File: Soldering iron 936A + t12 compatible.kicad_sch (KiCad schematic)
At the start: 62 parts, among them J1 DC INPUT, J2 OLED, J3 AC input, J4 output_connector, J5 mosfet_driver_future_backup, Q1 IRF9540N, Q2 BC547, SW1 RotaryEncoder_Switch, U1 LM2596S-ADJ, U2 LM358

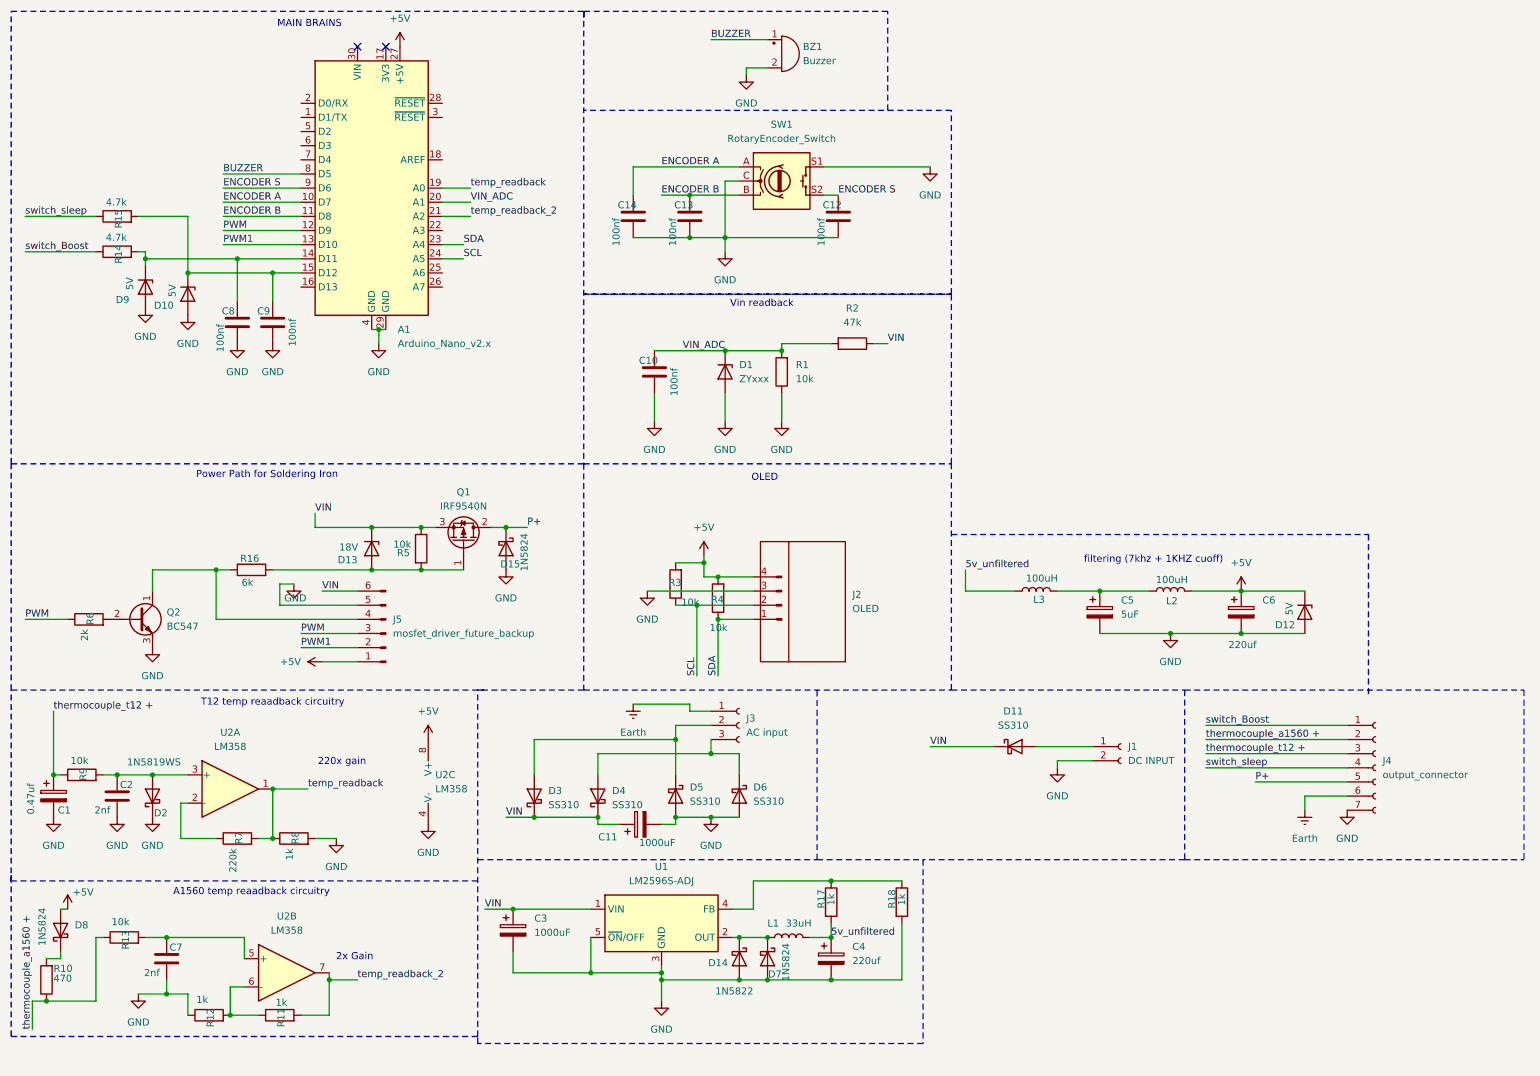
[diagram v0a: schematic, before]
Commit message: PCB arrived , T12 verified , code updating , Fixed mistakes and redid schmatic
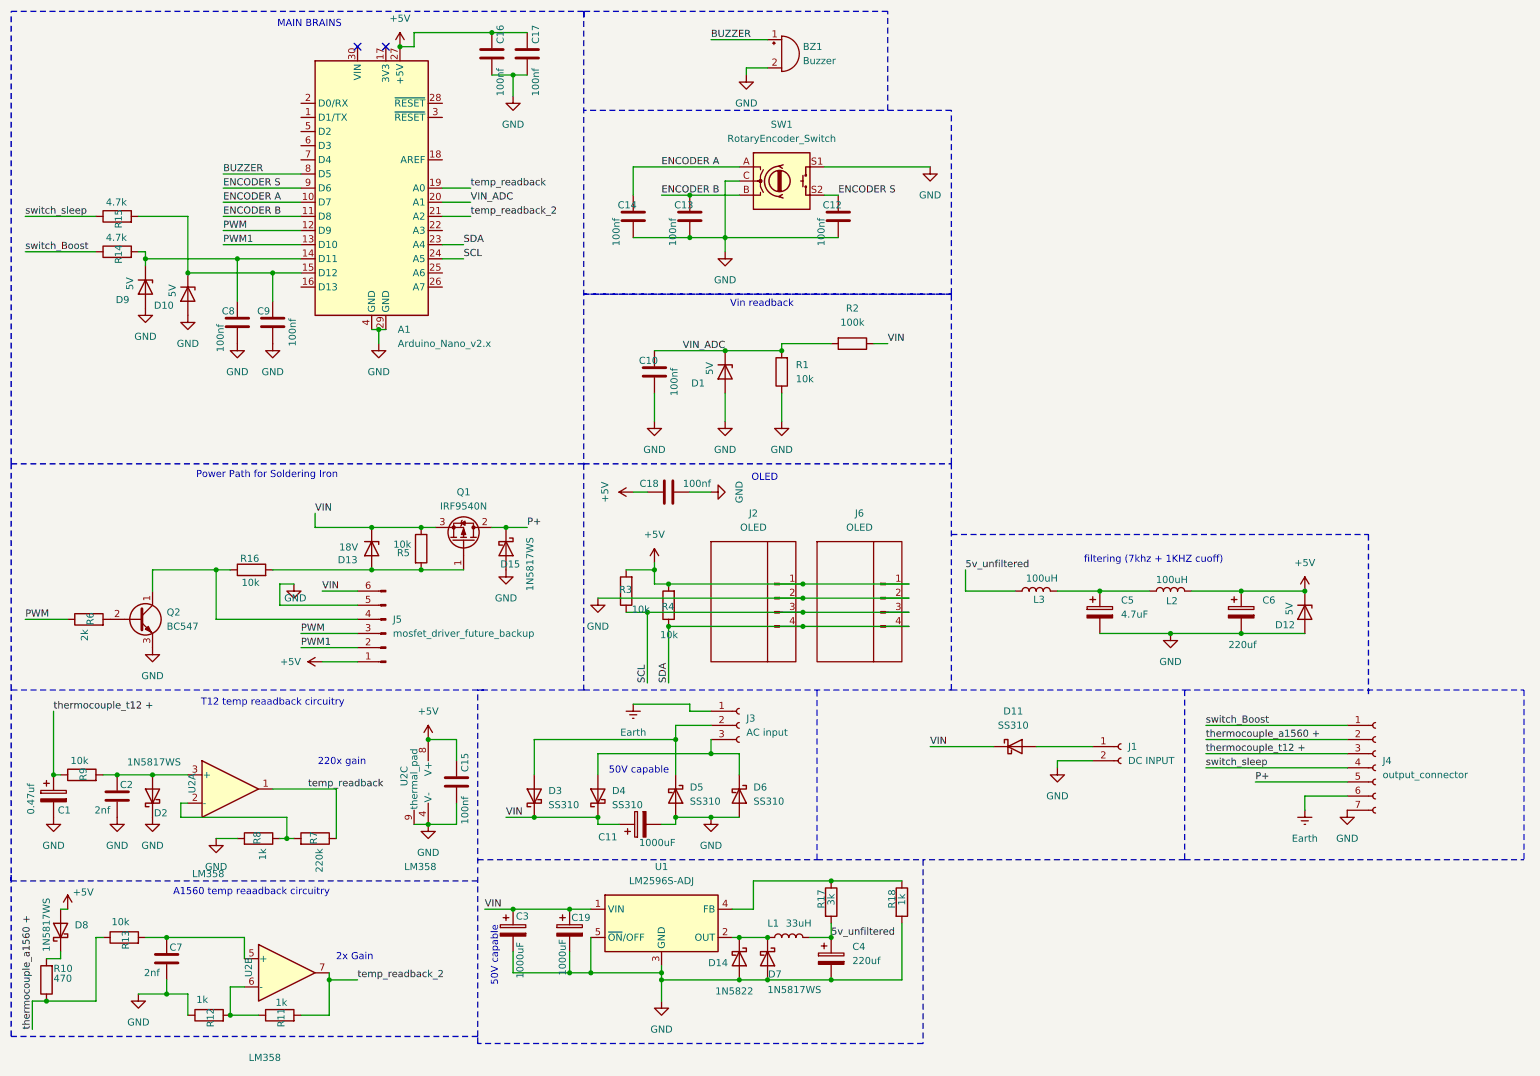
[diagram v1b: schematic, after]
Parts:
- removed D1: ZYxxx, Diode_THT:D_DO-41_SOD81_P10.16mm_Horizontal, symbol Diode:ZYxxx
- added C15, C16, C17, C18: 100nf, Capacitor_SMD:C_0603_1608Metric_Pad1.08x0.95mm_HandSolder, symbol Device:C
- added C19: 1000uF, Capacitor_THT:CP_Radial_D10.0mm_P5.00mm, symbol Device:C_Polarized
- added D1: 5V, Diode_THT:D_A-405_P10.16mm_Horizontal, symbol Device:D_Zener
- added J6: OLED, Connector_PinHeader_2.54mm:PinHeader_1x04_P2.54mm_Vertical, symbol Connector:Conn_01x04_Pin
- C5: value 5uF -> 4.7uF
- D15, D7, D8: value 1N5824 -> 1N5817WS
- D2: value 1N5819WS -> 1N5817WS
- R16: value 6k -> 10k
- R17: value 1k -> 3k
- R2: value 47k -> 100k
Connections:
- net +5V: now also J2.1 (SDA), C15.1, C16.1, C17.1, C18.1, J6.1 (SDA); no longer J2.4 (VDD)
- net GND: now also J2.2 (SCL), U2.9 (thermal_pad), C15.2, C16.2, C17.2, C18.2, C19.2, D1.2 (A), J6.2 (SCL); no longer J2.3 (GND)
- net SCL: now also J2.3 (GND), J6.3 (GND); no longer J2.2 (SCL)
- net SDA: now also J2.4 (VDD), J6.4 (VDD); no longer J2.1 (SDA)
- net VIN: now also C19.1
- net VIN_ADC: now also D1.1 (K)
- net temp_readback: now also R7.1; no longer R7.2, R8.1
- net at U2.2 (-): now also R7.2, R8.1; no longer R7.1
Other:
- note added: "50V capable"
- moved on the sheet: J2, R3, R4, R7, R8

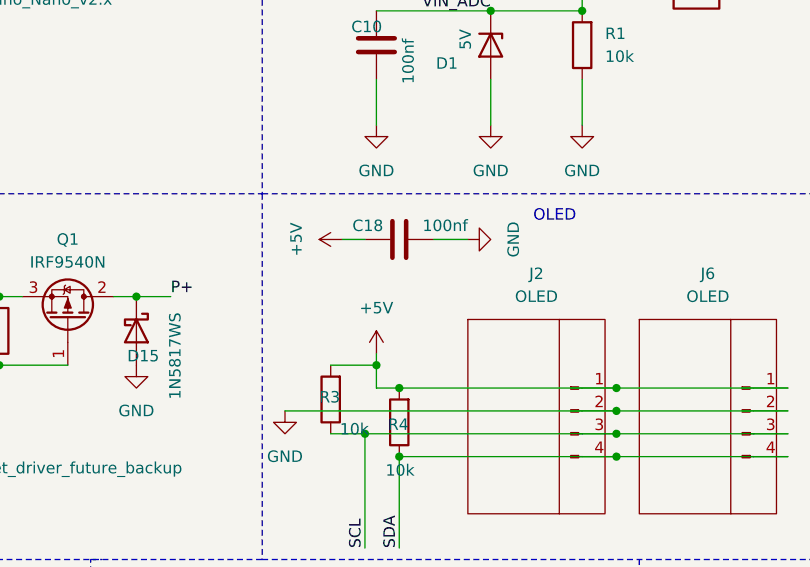
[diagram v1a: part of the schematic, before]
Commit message: added BOM generation + decoupling Cap for other orination of OLED , Fixed PCB orientation in Readme
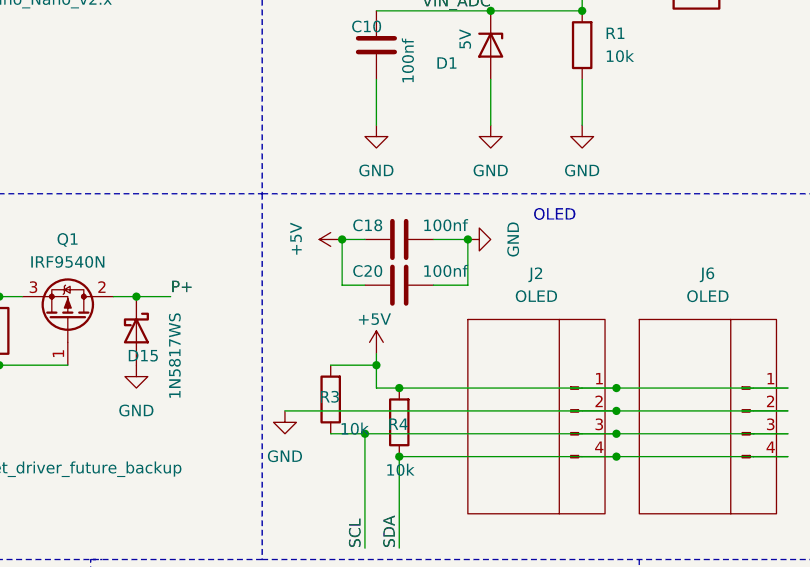
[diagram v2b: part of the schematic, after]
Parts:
- added C20: 100nf, Capacitor_SMD:C_0603_1608Metric_Pad1.08x0.95mm_HandSolder, symbol Device:C
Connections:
- net +5V: now also C20.1
- net GND: now also C20.2
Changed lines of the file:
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@@
 	)
 	(junction
+		(at 138.43 99.06)
+		(diameter 0)
+		(color 0 0 0 0)
+	)
+	(junction
 		(at 132.08 157.48)
 		(diameter 0)
@@
 	)
 	(junction
+		(at 124.46 99.06)
+		(diameter 0)
+		(color 0 0 0 0)
+	)
+	(junction
 		(at 127 120.65)
 		(diameter 0)
@@
 	(wire
 		(pts
+			(xy 127 104.14) (xy 124.46 104.14)
+		)
+		(stroke
+			(width 0)
+			(type default)
+		)
+	)
+	(wire
+		(pts
 			(xy 15.24 49.53) (xy 27.94 49.53)
 		)
@@
 	(wire
 		(pts
+			(xy 138.43 104.14) (xy 138.43 99.06)
+		)
+		(stroke
+			(width 0)
+			(type default)
+		)
+	)
+	(wire
+		(pts
 			(xy 36.83 57.15) (xy 53.34 57.15)
 		)
@@
 	(wire
 		(pts
+			(xy 124.46 104.14) (xy 124.46 99.06)
+		)
+		(stroke
+			(width 0)
+			(type default)
+		)
+	)
+	(wire
+		(pts
 			(xy 40.64 186.69) (xy 40.64 189.23)
 		)
@@
 	(wire
 		(pts
+			(xy 134.62 104.14) (xy 138.43 104.14)
+		)
+		(stroke
+			(width 0)
+			(type default)
+		)
+	)
+	(wire
+		(pts
 			(xy 59.69 59.69) (xy 64.77 59.69)
 		)
@@
 		(on_board yes)
 		(dnp no)
-		(fields_autoplaced yes)
 		(property "Reference" "#PWR09"
 			(at 128.27 115.57 0)
@@
 		)
 		(property "Value" "+5V"
-			(at 128.27 106.68 0)
+			(at 128.016 107.95 0)
 			(effects
 				(font
@@
 					(unit 1)
 				)
+			)
+		)
+	)
+	(symbol
+		(lib_id "Device:C")
+		(at 130.81 104.14 90)
+		(unit 1)
+		(exclude_from_sim no)
+		(in_bom yes)
+		(on_board yes)
+		(dnp no)
+		(property "Reference" "C20"
+			(at 129.032 102.616 90)
+			(effects
+				(font
+					(size 1.27 1.27)
+				)
+				(justify left)
+			)
+		)
+		(property "Value" "100nf"
+			(at 138.43 102.616 90)
+			(effects
+				(font
+					(size 1.27 1.27)
+				)
+				(justify left)
+			)
+		)
+		(property "Footprint" "Capacitor_SMD:C_0603_1608Metric_Pad1.08x0.95mm_HandSolder"
+			(at 134.62 103.1748 0)
+			(effects
+				(font
+					(size 1.27 1.27)
+				)
+				(hide yes)
+			)
+		)
+		(property "Datasheet" "~"
+			(at 130.81 104.14 0)
+			(effects
+				(font
+					(size 1.27 1.27)
+				)
+				(hide yes)
+			)
+		)
+		(property "Description" "Unpolarized capacitor"
+			(at 130.81 104.14 0)
+			(effects
+				(font
+					(size 1.27 1.27)
+				)
+				(hide yes)
+			)
+		)
+		(pin "1"
+		)
+		(pin "2"
+		)
+		(instances
+			(project "Soldering iron 936A + t12 compatible"
+				(path "/7b8f23b9-5775-45f1-8dbe-ed5fada41d3e"
+					(reference "C20")
+					(unit 1)
+				)

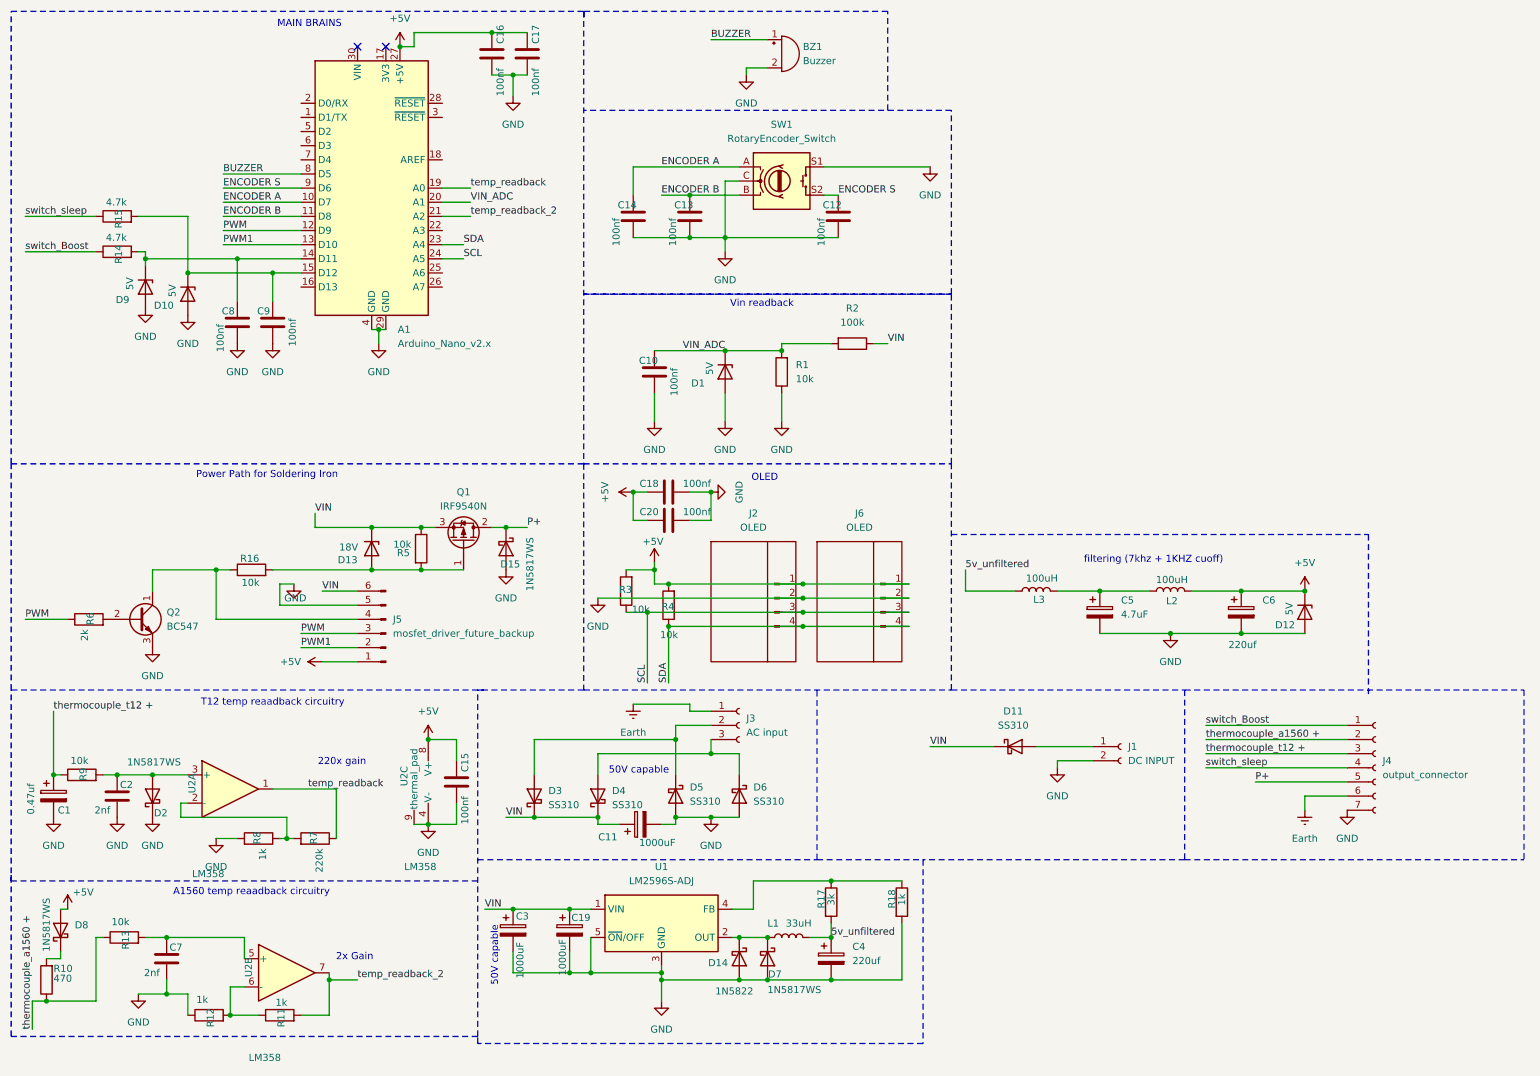
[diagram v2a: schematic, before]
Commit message: Updated schematic but have to update layout , foot prints ,add mosfet driver for 31 KHZ driving
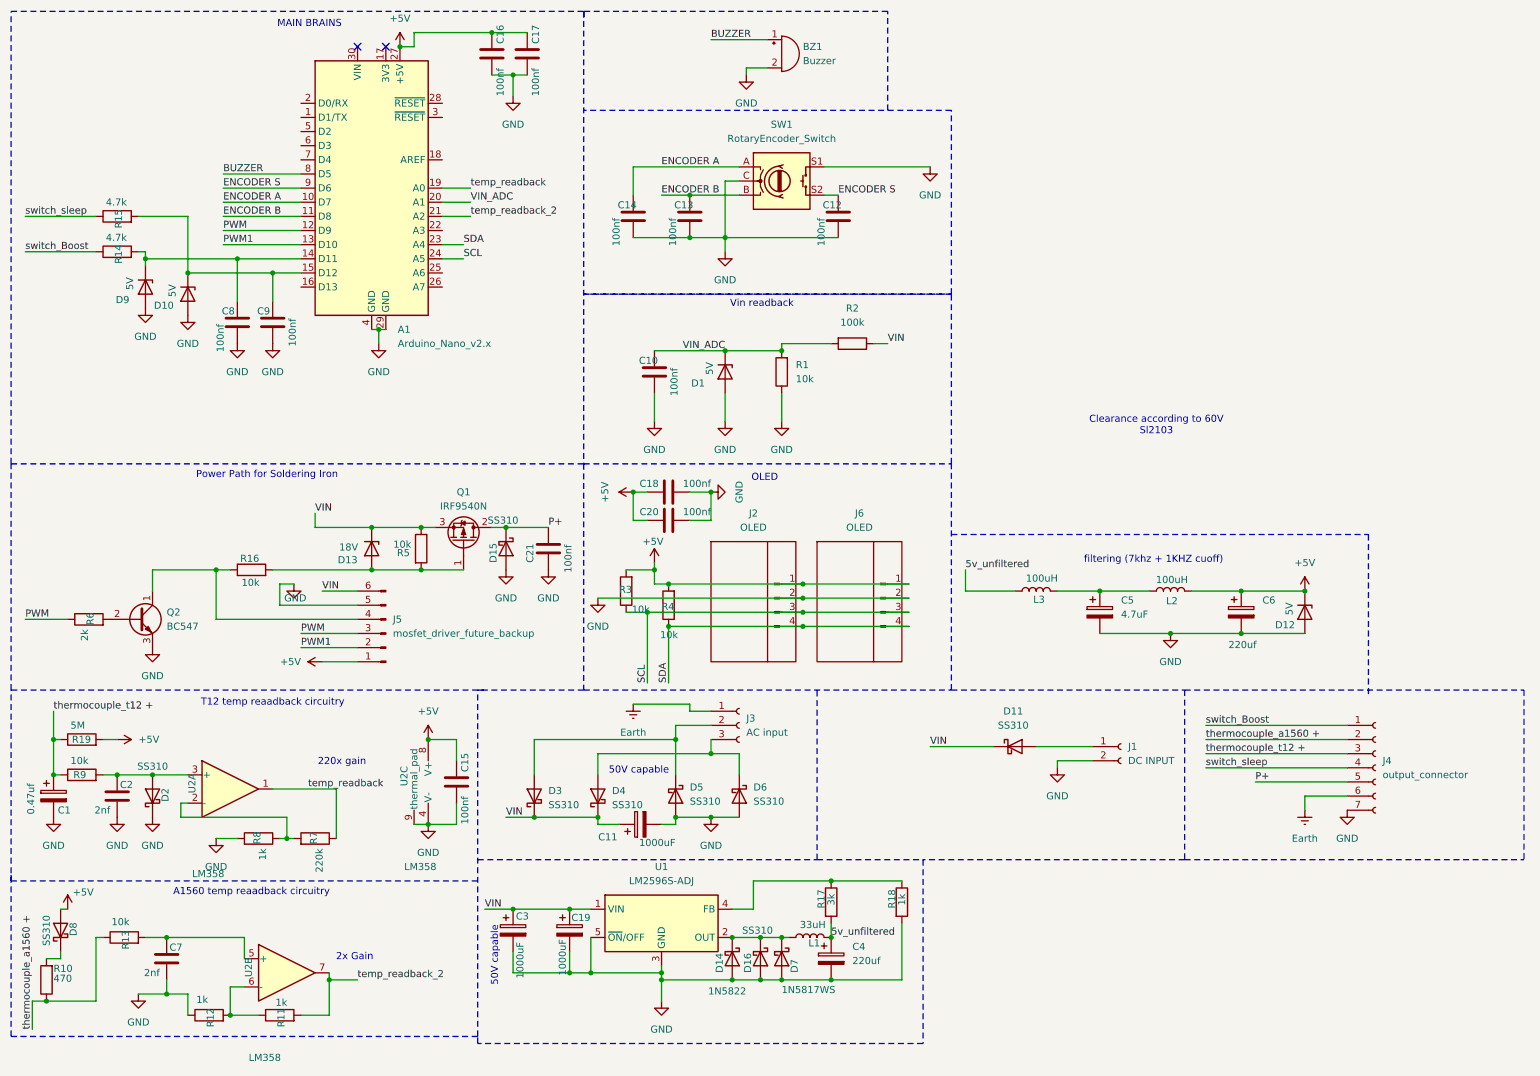
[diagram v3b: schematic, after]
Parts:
- removed D15, D2, D8: 1N5817WS, Diode_SMD:D_SOD-323, symbol Diode:1N5819WS
- added C21: 100nf, Capacitor_SMD:C_0603_1608Metric_Pad1.08x0.95mm_HandSolder, symbol Device:C
- added D15, D16, D2, D8: SS310, Diode_SMD:D_SMA, symbol Diode:SS310
- added R19: 5M, Resistor_SMD:R_1206_3216Metric_Pad1.30x1.75mm_HandSolder, symbol Device:R
- C11, C19, C3: footprint Capacitor_THT:CP_Radial_D10.0mm_P5.00mm -> Capacitor_THT:CP_Radial_D16.0mm_P7.50mm
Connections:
- net +5V: now also D8.2 (A), R19.2
- net GND: now also C21.2, D15.2 (A), D16.2 (A), D2.1 (K)
- net P+: now also C21.1, D15.1 (K)
- net thermocouple_t12 +: now also R19.1
- net at C2.1, R9.2, U2.3 (+): now also D2.2 (A)
- net at D14.1 (K), D7.1 (K), L1.1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: now also D16.1 (K)
- net at R10.2: now also D8.1 (K)
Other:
- note added: "Clearance according to 60V Sl2103"
- moved on the sheet: D14, D7, L1
